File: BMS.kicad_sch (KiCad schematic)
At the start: 63 parts, among them J1 Screw_Terminal_01x02, J5 BATT_PACK -, J6 BATT_PACK -, Q22 CSD19531Q5A, Q23 CSD19531Q5A, Q24 CSD19531Q5A, T3 EE20_10_6_750811647, U1 TL431DBZ, U18 VIPer26LD, U2 PC817, U21 BQ7790500PWR

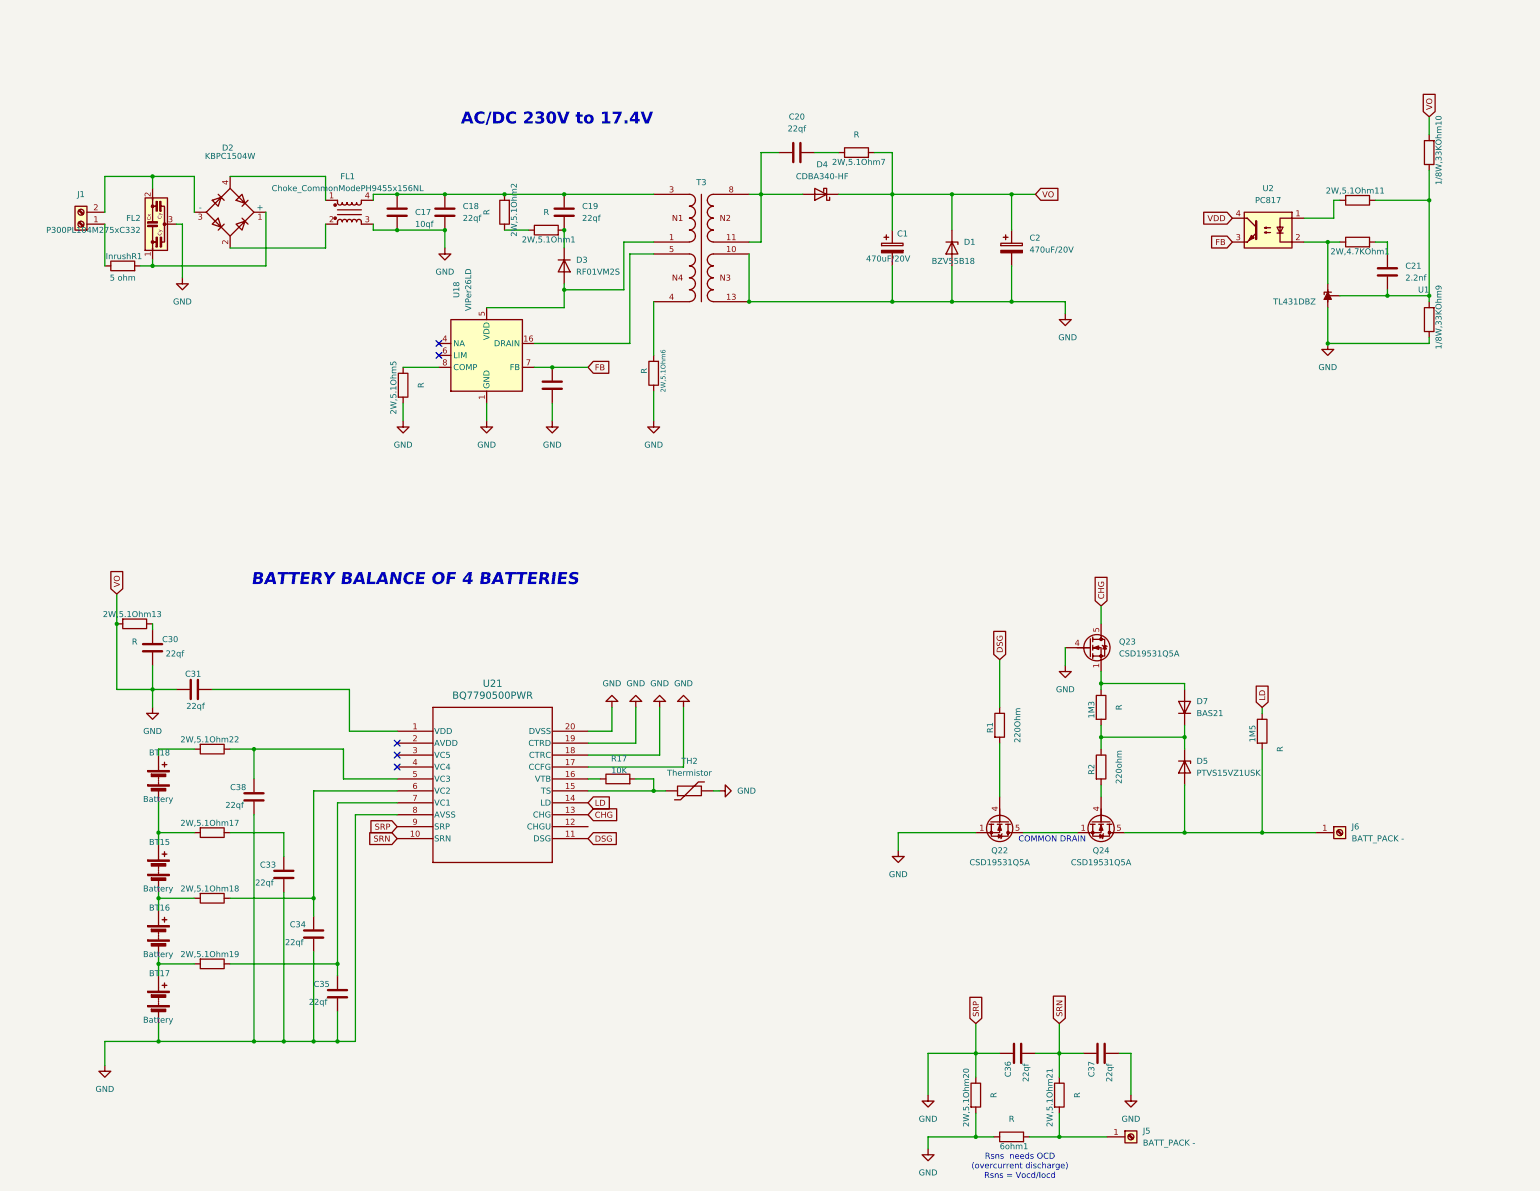
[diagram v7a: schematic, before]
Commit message: Add Wurth connector 3D model & footprint
Add STEP 3D model and footprint for T_Wurth_WE-OLTI-EE20_10_6_750811647 and update KiCad project files. BMS.kicad_pro and BMS.kicad_sch were modified, autosave schematic files removed, and backup ZIPs (BMS-backups) and editor lock files were added as part of the change.
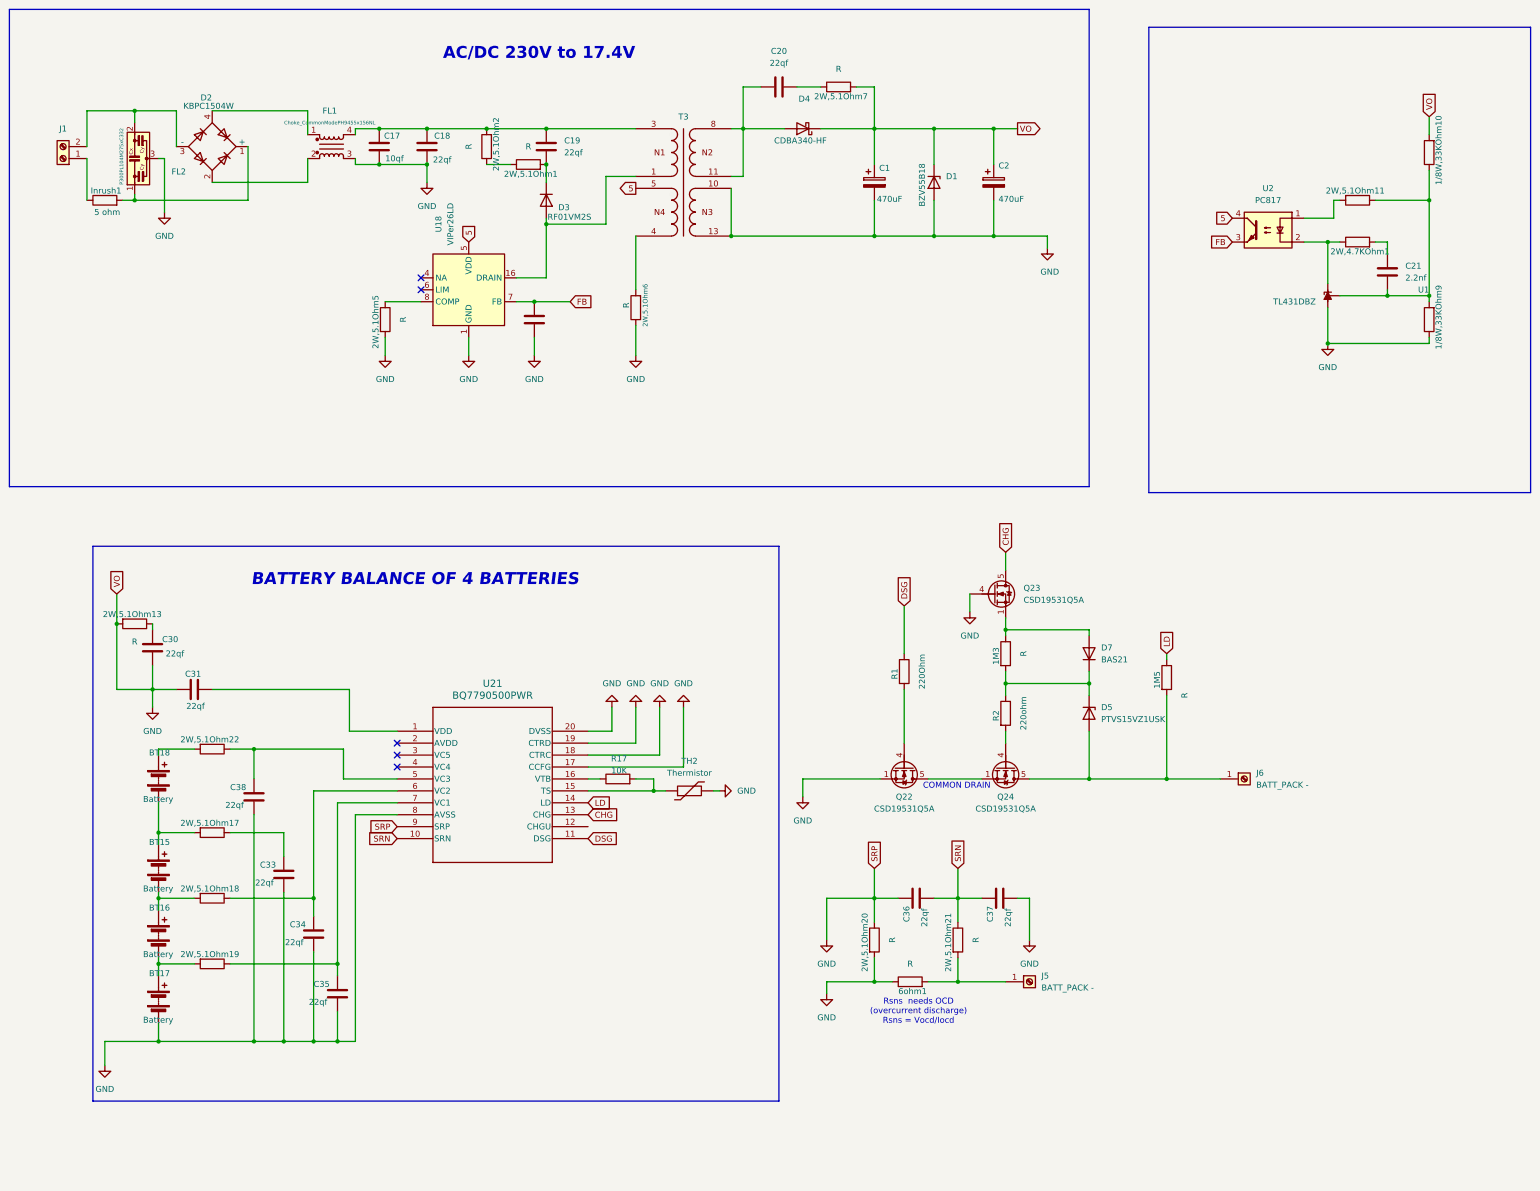
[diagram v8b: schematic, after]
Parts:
- 1/8W,33KOhm10, 1/8W,33KOhm9, 1M3, 1M5, 2W,4.7KOhm1, 2W,5.1Ohm1, 2W,5.1Ohm11, 2W,5.1Ohm13, 2W,5.1Ohm17, 2W,5.1Ohm18, 2W,5.1Ohm19, 2W,5.1Ohm2, 2W,5.1Ohm20, 2W,5.1Ohm21, 2W,5.1Ohm22, 2W,5.1Ohm5, 2W,5.1Ohm6, 2W,5.1Ohm7, 6ohm1: footprint Resistor_THT:R_Axial_DIN0414_L11.9mm_D4.5mm_P15.24mm_Horizontal -> Resistor_SMD:R_0603_1608Metric
- C1, C2: value 470uF/20V -> 470uF
- J1: footprint (none) -> TerminalBlock_MetzConnect:TerminalBlock_MetzConnect_360291_1x01_Horizontal_ScrewM3.0_Boxed
- J5, J6: footprint (none) -> TerminalBlock_MetzConnect:TerminalBlock_MetzConnect_360271_1x01_Horizontal_ScrewM3.0_Boxed
- T3: footprint Transformer_THT_Wurth:T_Wurth_WE-OLTI-EE20_10_6_750811647 -> Transformer_THT:Transformer_Wuerth_760871131
- renumbered InrushR1 to Inrush1
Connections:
- net at D3.2 (A), T3.1: now also U18.13 (DRAIN), U18.14 (DRAIN), U18.15 (DRAIN), U18.16 (DRAIN); no longer U18.5 (VDD)
- net VDD renamed 5
- net 5: now also T3.5, U18.5 (VDD)
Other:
- moved on the sheet: 1M3, 1M5, 2W,5.1Ohm1, 2W,5.1Ohm2, 2W,5.1Ohm20, 2W,5.1Ohm21, 2W,5.1Ohm5, 2W,5.1Ohm6, 2W,5.1Ohm7, 6ohm1, C1, C17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
